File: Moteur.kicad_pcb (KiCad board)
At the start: 4 copper layers, 31.8 x 16 mm, 53 parts, among them IC1 TPS71501, IC2 TLV710, IC3 MAX3051, IC4 LM5106, IC5 LM5106, IC6 INA282, P1 Bus2, P2 CONN_6, P3 GPIO, P4 CONN_1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

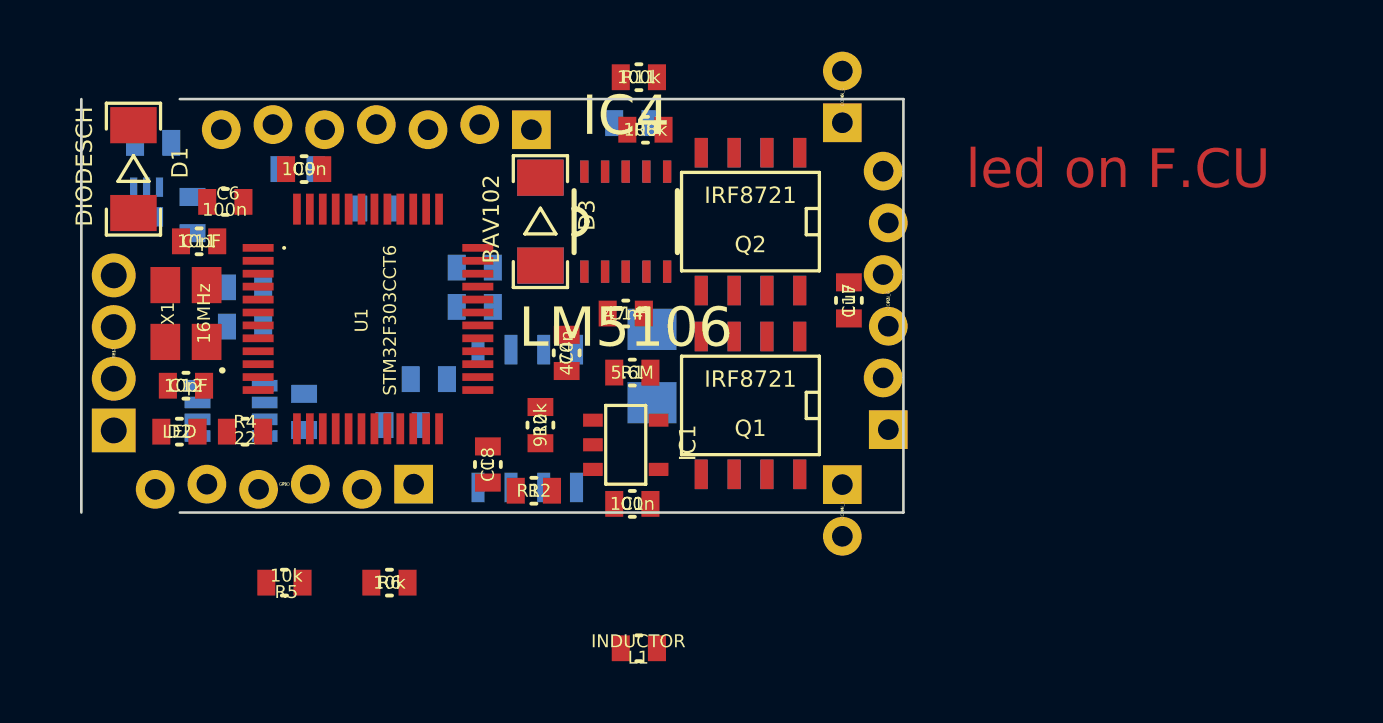
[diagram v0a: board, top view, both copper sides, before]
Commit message: component placement
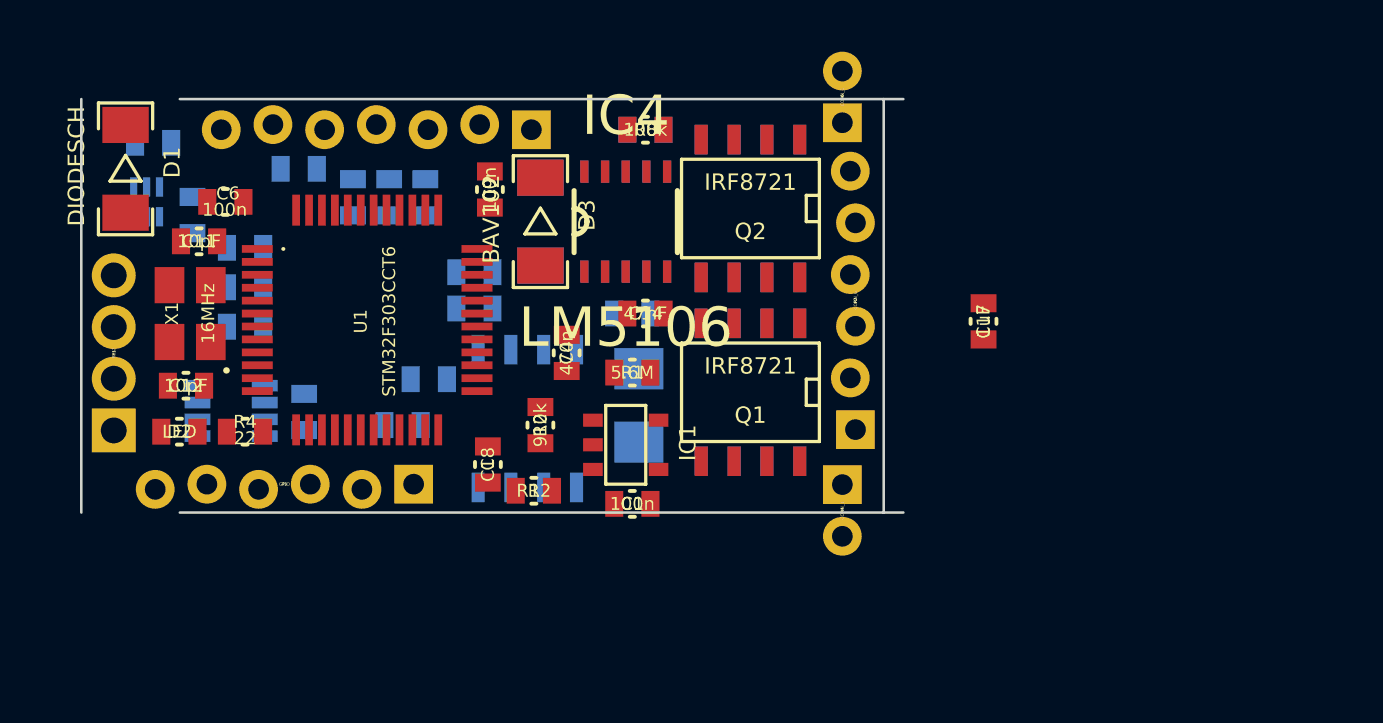
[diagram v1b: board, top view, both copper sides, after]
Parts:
- L1, R11, R5, R6: moved to B.Cu
- moved L1 21.7 mm to (128.5, 95.8)
- moved R5 15.5 mm to (134.1, 93.8), turned to 270 degrees
- moved R6 15.0 mm to (135.5, 93.8), turned to 270 degrees
- moved R11 9.15 mm to (143.5, 98.3)
- moved C9 7.23 mm to (138.0, 93.5), turned to 90 degrees
- moved C17 5.27 mm to (157.1, 98.6)
- moved R10 1.61 mm to (143.8, 101.9)
- moved P2 1.27 mm to (152.1, 97.8)
- moved R3 1.00 mm to (132.7, 93.8), turned to 270 degrees
- moved C14 0.76 mm to (144.0, 98.3)
- moved C16 0.57 mm to (144.0, 91.2)
- moved Q2 0.51 mm to (148.1, 94.2)
- moved Q4 0.51 mm to (148.1, 94.2)
- moved Q1 0.51 mm to (148.1, 101.3)
- moved Q3 0.51 mm to (148.1, 101.3)
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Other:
- outline, holes or cut-outs redrawn
- board text removed: "led on F.CU"

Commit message: component placement
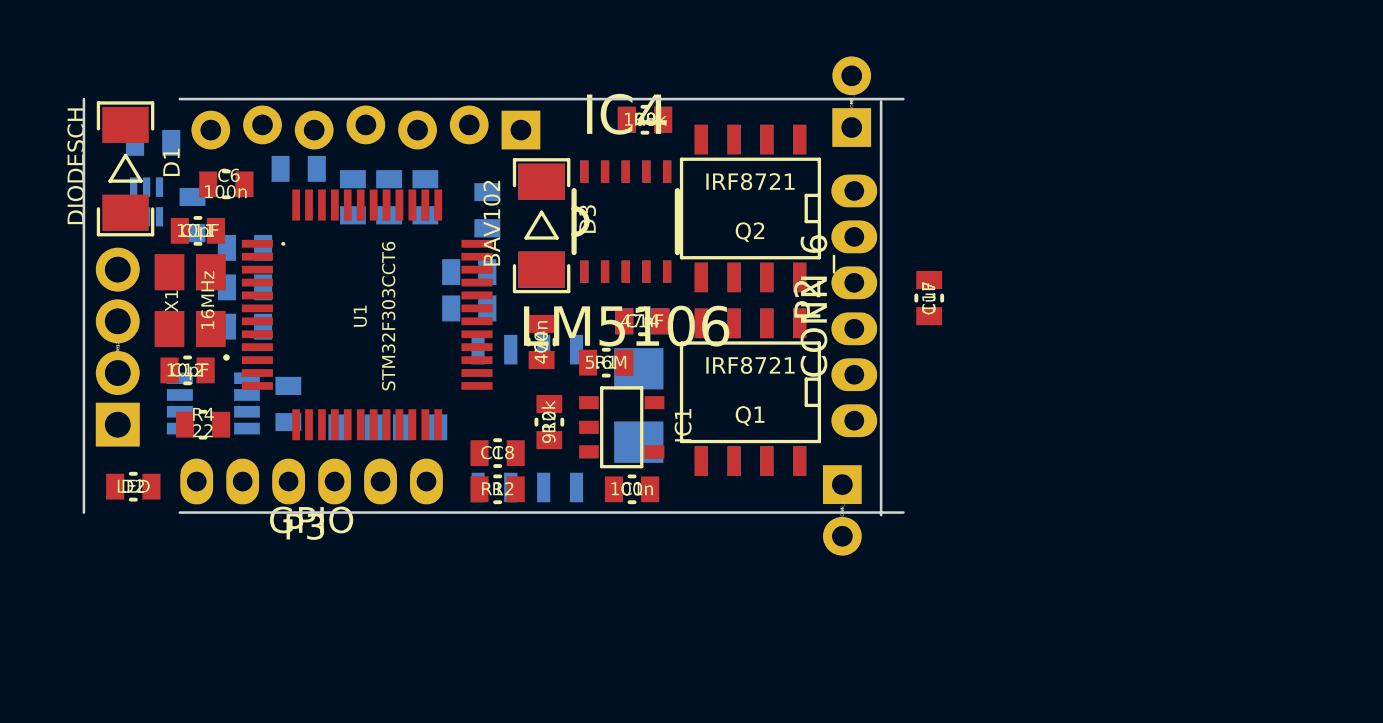
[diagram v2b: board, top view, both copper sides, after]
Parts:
- C9: moved to B.Cu
- P2, P3: footprint _Pin2mm_6z -> ribbon_cable_6pin
- moved D2 2.78 mm to (124.2, 105.0)
- moved C17 2.28 mm to (155.0, 97.7)
- moved C7 1.89 mm to (135.3, 102.7)
- moved R13 1.82 mm to (132.8, 102.7)
- moved R4 1.65 mm to (126.9, 102.6)
- moved R12 1.40 mm to (138.3, 105.1)
- moved R1 1.08 mm to (142.5, 100.2)
- moved C4 1.06 mm to (140.0, 99.4)
- moved P3 1.06 mm to (131.1, 104.8)
- moved C9 0.81 mm to (137.9, 94.3)
- moved IC3 0.75 mm to (128.6, 100.8)
- moved IC1 0.70 mm to (143.1, 102.7)
- moved C13 0.68 mm to (130.2, 101.8)
- moved C6 0.68 mm to (127.8, 93.3)
- moved C12 0.60 mm to (126.3, 100.5)
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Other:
- board size 31.8 x 16 mm -> 31.7 x 16.1 mm

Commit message: optimize placement
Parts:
- C17: moved to B.Cu
- moved C17 29.3 mm to (126.2, 102.9), turned to 0 degrees
- moved C2 13.2 mm to (123.6, 104.8), turned to 180 degrees
- moved D1 10.0 mm to (123.5, 102.7), turned to 90 degrees
- moved IC2 8.87 mm to (123.8, 102.8), turned to 180 degrees
- moved IC3 7.91 mm to (128.2, 92.9)
- moved C13 7.11 mm to (129.8, 94.7)
- moved C3 6.55 mm to (123.9, 100.5), turned to 180 degrees
- moved P1 4.60 mm to (123.4, 95.0), turned to 270 degrees
- moved D2 3.08 mm to (126.0, 102.5), turned to 270 degrees
- moved L1 2.24 mm to (126.9, 97.3)
- moved C8 2.22 mm to (126.9, 98.8)
- moved C10 2.09 mm to (127.3, 100.5)
- moved P3 1.00 mm to (130.1, 104.8)
- moved P5 1.00 mm to (132.2, 91.2)
- moved R4 0.51 mm to (127.4, 102.5), turned to 270 degrees
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
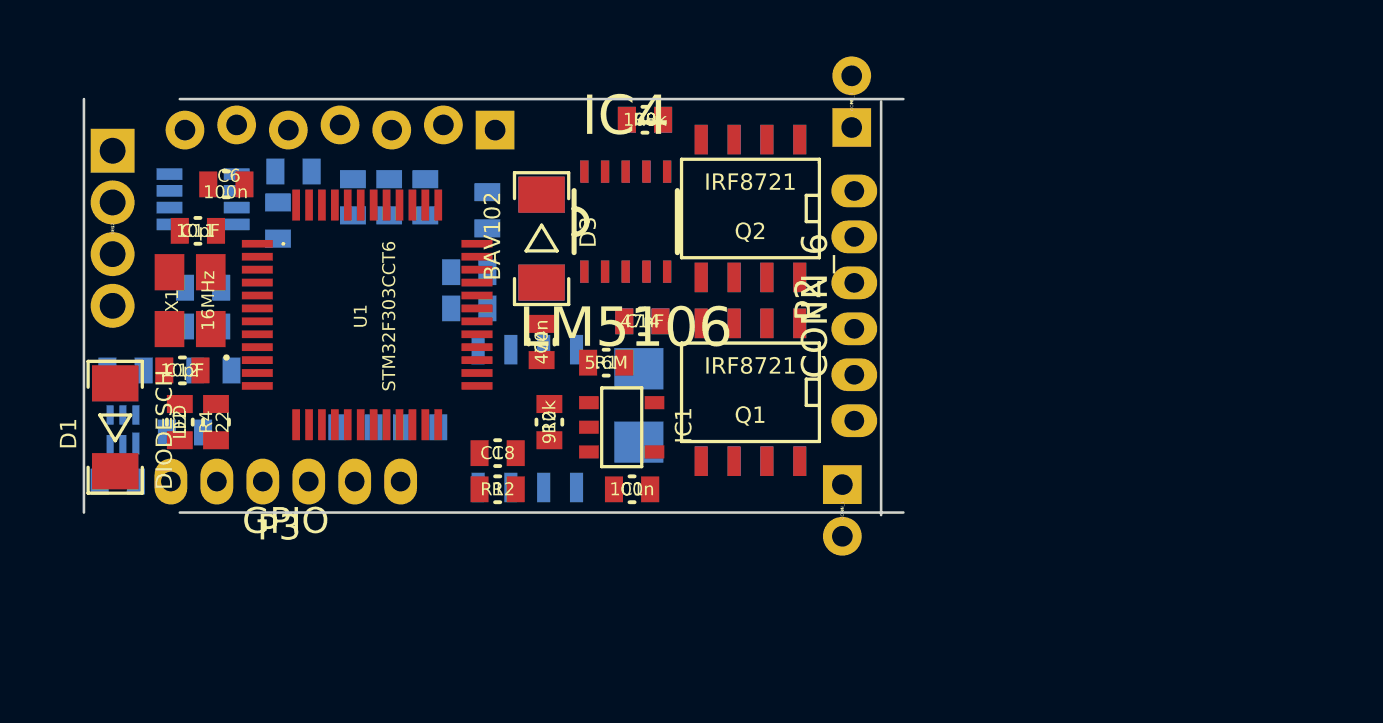
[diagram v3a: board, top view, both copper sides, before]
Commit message: add new gpio connector with gnd
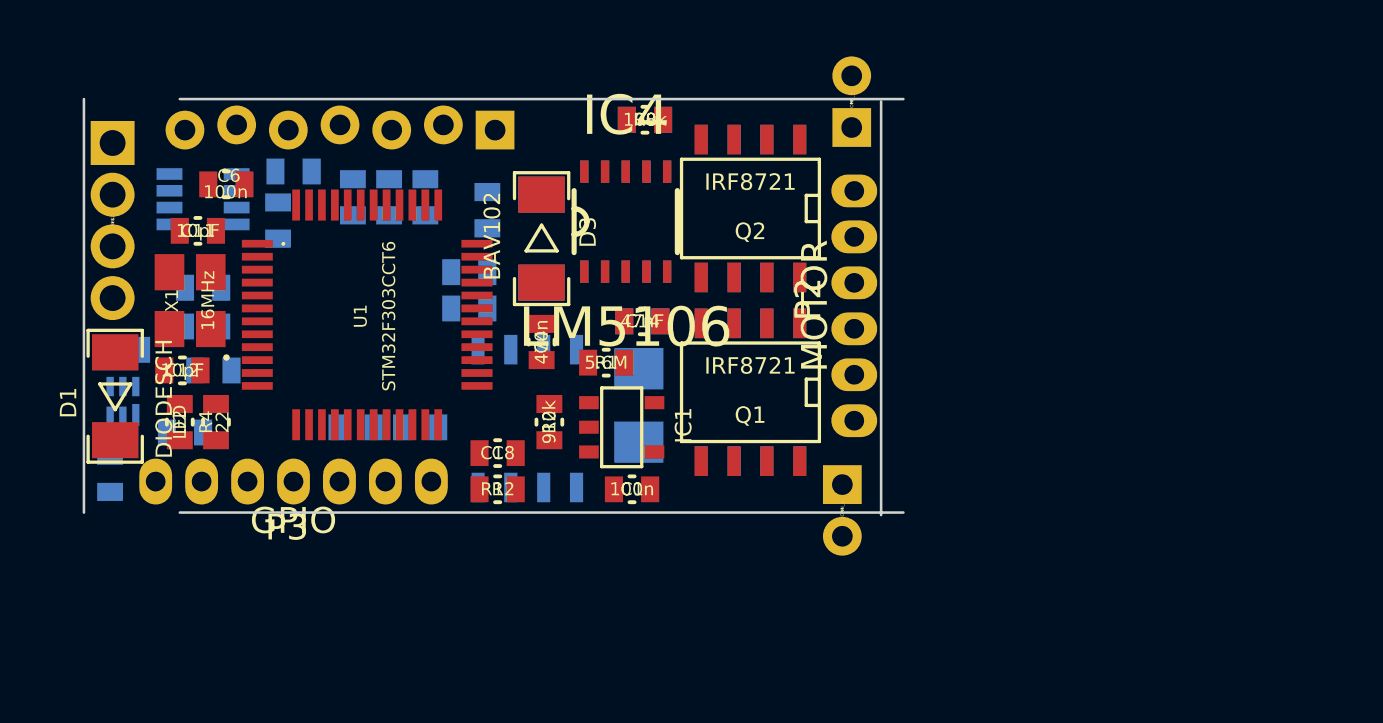
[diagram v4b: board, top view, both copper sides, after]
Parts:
- P2: value CONN_6 -> MOTOR
- P3: footprint ribbon_cable_6pin -> ribbon_cable_7pin
- moved D1 1.20 mm to (123.5, 101.5)
- moved IC2 1.10 mm to (123.8, 101.7)
- moved C3 0.81 mm to (123.8, 99.7)
- moved C2 0.42 mm to (123.3, 104.5), turned to 90 degrees
- moved P3 0.30 mm to (130.4, 104.8)
- moved P1 0.30 mm to (123.4, 94.7)
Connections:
- P1 pad 1: CANL -> CANH
- P1 pad 2: CANH -> CANL
- P3 pad 5: +3.3V_A -> GND
- P3 pad 6: +5V_protected -> +3.3V_A

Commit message: start routing
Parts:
- moved R6 3.67 mm to (133.9, 97.1), turned to 0 degrees
- moved C5 1.28 mm to (131.2, 93.8), turned to 270 degrees
- moved R3 0.40 mm to (132.7, 94.2)
- moved R5 0.40 mm to (134.1, 94.2)
- moved C6 0.40 mm to (127.4, 93.3)
- moved C13 0.30 mm to (129.8, 94.4)
- moved C12 0.22 mm to (126.2, 100.3)
- moved X1 0.20 mm to (126.4, 97.6)
- moved C11 0.20 mm to (126.7, 94.9)
- moved IC3 0.10 mm to (128.3, 92.9)
- moved D2 0.10 mm to (126.0, 102.4)
- moved R4 0.10 mm to (127.4, 102.4)
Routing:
- net Swdio: track 0.00 -> 9.32 mm, vias 0 -> 1
- net +3.3V: track 0.00 -> 8.07 mm, vias 0 -> 2
- net CAN_SPEED: track 0.00 -> 7.11 mm
- net N-0000041: track 0.00 -> 6.15 mm, vias 0 -> 1
- net N-0000040: track 0.00 -> 4.85 mm, vias 0 -> 1
- net N-0000065: track 0.00 -> 4.03 mm
- net N-0000064: track 0.00 -> 3.77 mm
- net Swdclk: track 0.00 -> 3.65 mm
- net CANH: track 0.00 -> 3.18 mm
- net CANL: track 0.00 -> 2.51 mm
- net LED: track 0.00 -> 2.29 mm
- net Reset: track 0.00 -> 1.57 mm, vias 0 -> 1
- net N-0000038: track 0.00 -> 1.40 mm

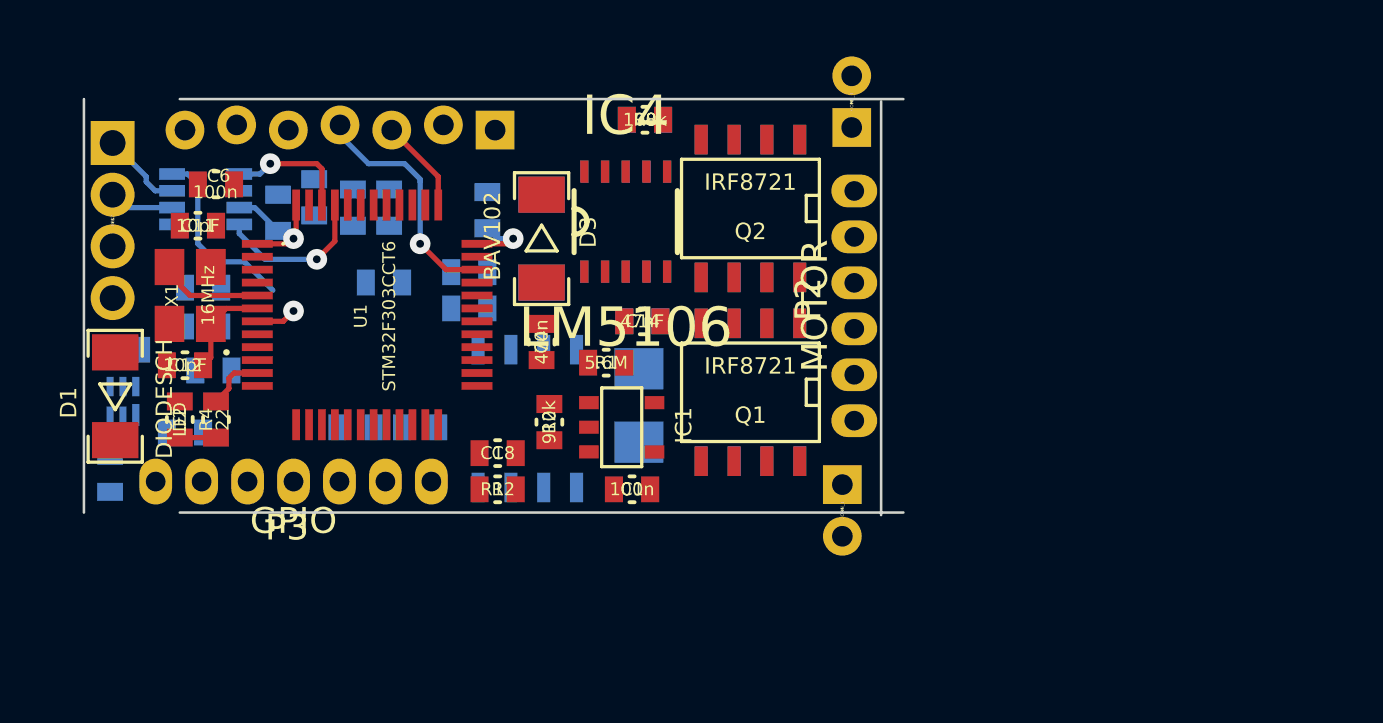
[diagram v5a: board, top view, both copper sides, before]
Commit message: routing, exchanged shunt resistor pins
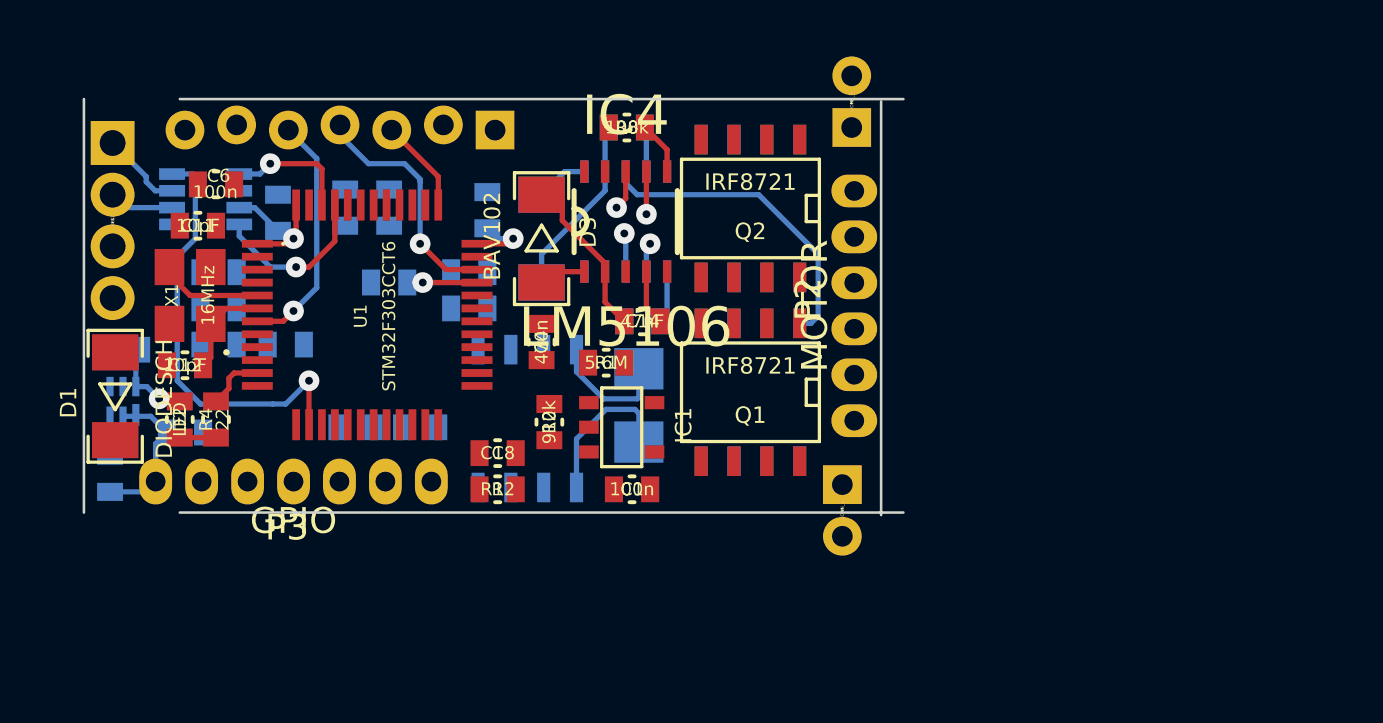
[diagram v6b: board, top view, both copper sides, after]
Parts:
- moved C5 4.70 mm to (127.5, 96.7), turned to 180 degrees
- moved L1 3.88 mm to (130.1, 99.5), turned to 180 degrees
- moved R5 1.70 mm to (132.4, 94.2)
- moved R3 1.40 mm to (134.1, 94.2)
- moved C10 1.02 mm to (127.5, 99.5)
- moved C8 0.92 mm to (127.5, 98.1)
- moved C16 0.76 mm to (143.3, 91.1)
- moved R8 0.76 mm to (143.3, 91.1)
- moved R6 0.20 mm to (134.1, 97.1)
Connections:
- C16 pad 2: N-0000044 (its old number) -> N-0000047
- IC5 pad 4: N-0000044 (its old number) -> N-0000047
- IC6 pad 1: N-0000044 (its old number) -> Mot-
- IC6 pad 8: Mot- -> N-0000047
- Q3 pad 1: N-0000044 (its old number) -> N-0000047
- Q3 pad 2: N-0000044 (its old number) -> N-0000047
- Q3 pad 3: N-0000044 (its old number) -> N-0000047
- Q4 pad 5: N-0000044 (its old number) -> N-0000047
- Q4 pad 6: N-0000044 (its old number) -> N-0000047
- Q4 pad 7: N-0000044 (its old number) -> N-0000047
- Q4 pad 8: N-0000044 (its old number) -> N-0000047
- R10 pad 2: N-0000044 (its old number) -> N-0000047
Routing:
- net N-0000048: track 0.00 -> 12.3 mm
- net CAN_SPEED: track 7.11 -> 16.7 mm, vias 0 -> 1
- net Reset: track 1.57 -> 9.39 mm
- net N-0000053: track 0.00 -> 7.08 mm
- net N-0000049: track 0.00 -> 6.69 mm
- net N-0000047: track 0.00 -> 6.56 mm
- net +5V_protected: track 0.00 -> 5.97 mm
- net Mot-: track 0.00 -> 5.94 mm
- net +9V: track 0.00 -> 3.86 mm
- net +3.3V: track 8.07 -> 11.5 mm, vias 2 -> 3
- net Mot+: track 0.00 -> 2.15 mm
- net I: track 0.00 -> 2.10 mm, vias 0 -> 1
- net N-0000051: track 0.00 -> 2.06 mm
- net N-0000055: track 0.00 -> 2.03 mm
- net Mot_En_1: track 0.00 -> 1.71 mm, vias 0 -> 1
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
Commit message: routing
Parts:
- moved C1 3.16 mm to (140.4, 104.5), turned to 90 degrees
- moved R1 1.32 mm to (141.2, 100.0), turned to 270 degrees
- moved R2 0.71 mm to (139.8, 102.0), turned to 180 degrees
- moved C14 0.61 mm to (143.3, 98.5)
- moved C4 0.57 mm to (139.6, 99.8)
- moved R8 0.20 mm to (143.3, 91.3)
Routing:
- net N-0000042: track 0.00 -> 7.50 mm
- net B: track 0.00 -> 1.87 mm, vias 0 -> 1

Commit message: routing (power)
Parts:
- C7, R13: moved to F.Cu
- moved C8 8.79 mm to (135.9, 100.7), turned to 90 degrees
- moved R13 7.64 mm to (140.2, 104.6), turned to 270 degrees
- moved L1 6.19 mm to (135.4, 102.7)
- moved C1 4.20 mm to (144.6, 104.7), turned to 270 degrees
- moved R12 4.14 mm to (142.4, 104.5)
- moved C7 2.64 mm to (137.4, 104.3), turned to 270 degrees
- moved C18 1.03 mm to (138.8, 104.6), turned to 270 degrees
- moved IC1 0.71 mm to (143.2, 102.0)
- moved R2 0.61 mm to (140.4, 101.9), turned to 270 degrees
- moved R1 0.60 mm to (141.2, 99.4)
- moved C4 0.40 mm to (139.6, 99.4)
- moved P3 0.32 mm to (130.1, 104.9)
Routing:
- net Mot+: track 1.85 -> 18.1 mm
- net N-0000047: track 6.56 -> 21.6 mm
- net ADC/V_BAT: track 0.00 -> 14.7 mm
- net +BATT: track 0.00 -> 13.4 mm
- net GND: track 0.00 -> 12.7 mm, vias 0 -> 1
- net +3.3V_A: track 0.00 -> 10.0 mm
- net Mot-: track 5.94 -> 14.9 mm
- net ADC/I_MOT: track 0.00 -> 7.31 mm
- net +3.3V: track 11.5 -> 15.5 mm, vias 3 -> 4
- net Tx: track 0.00 -> 2.41 mm, vias 0 -> 1
- net Rx: track 0.00 -> 2.05 mm, vias 0 -> 1
- net CAN_SPEED: track 16.7 -> 15.8 mm
